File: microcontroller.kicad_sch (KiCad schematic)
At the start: 0 parts

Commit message: top-level structure and ESP32-C6 pin assignments nearly sorted
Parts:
- added BT1: 18650, Battery:BatteryHolder_Keystone_1042_1x18650, symbol Device:Battery_Cell
- added C20: 100n, Capacitor_SMD:C_0603_1608Metric, symbol Device:C
- added J1: Micro_SD_Card 693072010801, Connector_Card:microSD_HC_Molex_47219-2001, symbol Connector:Micro_SD_Card
- added R11, R12: 4K7, Resistor_SMD:R_0603_1608Metric, symbol Device:R
- added R13, R14, R8, R9: 10k, Resistor_SMD:R_0603_1608Metric, symbol Device:R
- added U1: Seeed 113991254, Seeed:XIAO-ESP32-C6-SMD_PTH_DI, symbol OpenPolysom:XIAO-ESP32-C6-SMD
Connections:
- new net 3V3: C20.1, J1.4 (VDD), R11.1, R12.1, R8.1, R9.1, U1.12 (3V3), U1.22 (3V3)
- new net CLK_3: J1.5 (CLK), U1.19 (GPIO4_MTMS)
- new net CS_2: U1.2 (GPIO1_A1_D1)
- new net CS_3: J1.2 (DAT3/CD), U1.3 (GPIO2_A2_D2)
- new net DAT1: J1.8 (DAT1), R9.2
- new net DAT2: J1.1 (DAT2), R8.2
- new net GND: BT1.2 (-), C20.2, J1.6 (VSS), J1.SH (SHIELD), R14.2, U1.13 (GND), U1.18 (GND), U1.24 (GND)
- new net I2S_BCLK: U1.1 (GPIO0_A0_D0)
- new net I2S_DATA: U1.11 (GPIO18_D10_MOSI)
- new net I2S_MCLK: U1.16 (GPIO7_MTDO)
- new net I2S_WS: U1.8 (GPIO17_D7_RX)
- new net MISO_2: U1.10 (GPIO20_D9_MISO)
- new net MISO_3: J1.7 (DAT0), U1.15 (GPIO5_MTDI)
- new net MOSI_2: U1.4 (GPIO21_D3)
- new net MOSI_3: J1.3 (CMD), U1.20 (GPIO6_MTCK)
- new net PERIPH_EN: U1.7 (GPIO16_D6_TX)
- new net SCK_2: U1.9 (GPIO19_D8_SCK)
- new net SCL: R12.2, U1.6 (GPIO23_D5_SCL)
- new net SDA: R11.2, U1.5 (GPIO22_D4_SDA)
- new net VBAT: BT1.1 (+), R13.2, U1.23 (BAT)
- new net VBAT/2: R13.1, R14.1
- new net VBUS: U1.14 (VBUS)
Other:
- company: (none) -> Sunrise designs
- title: (none) -> Open polysomnography board

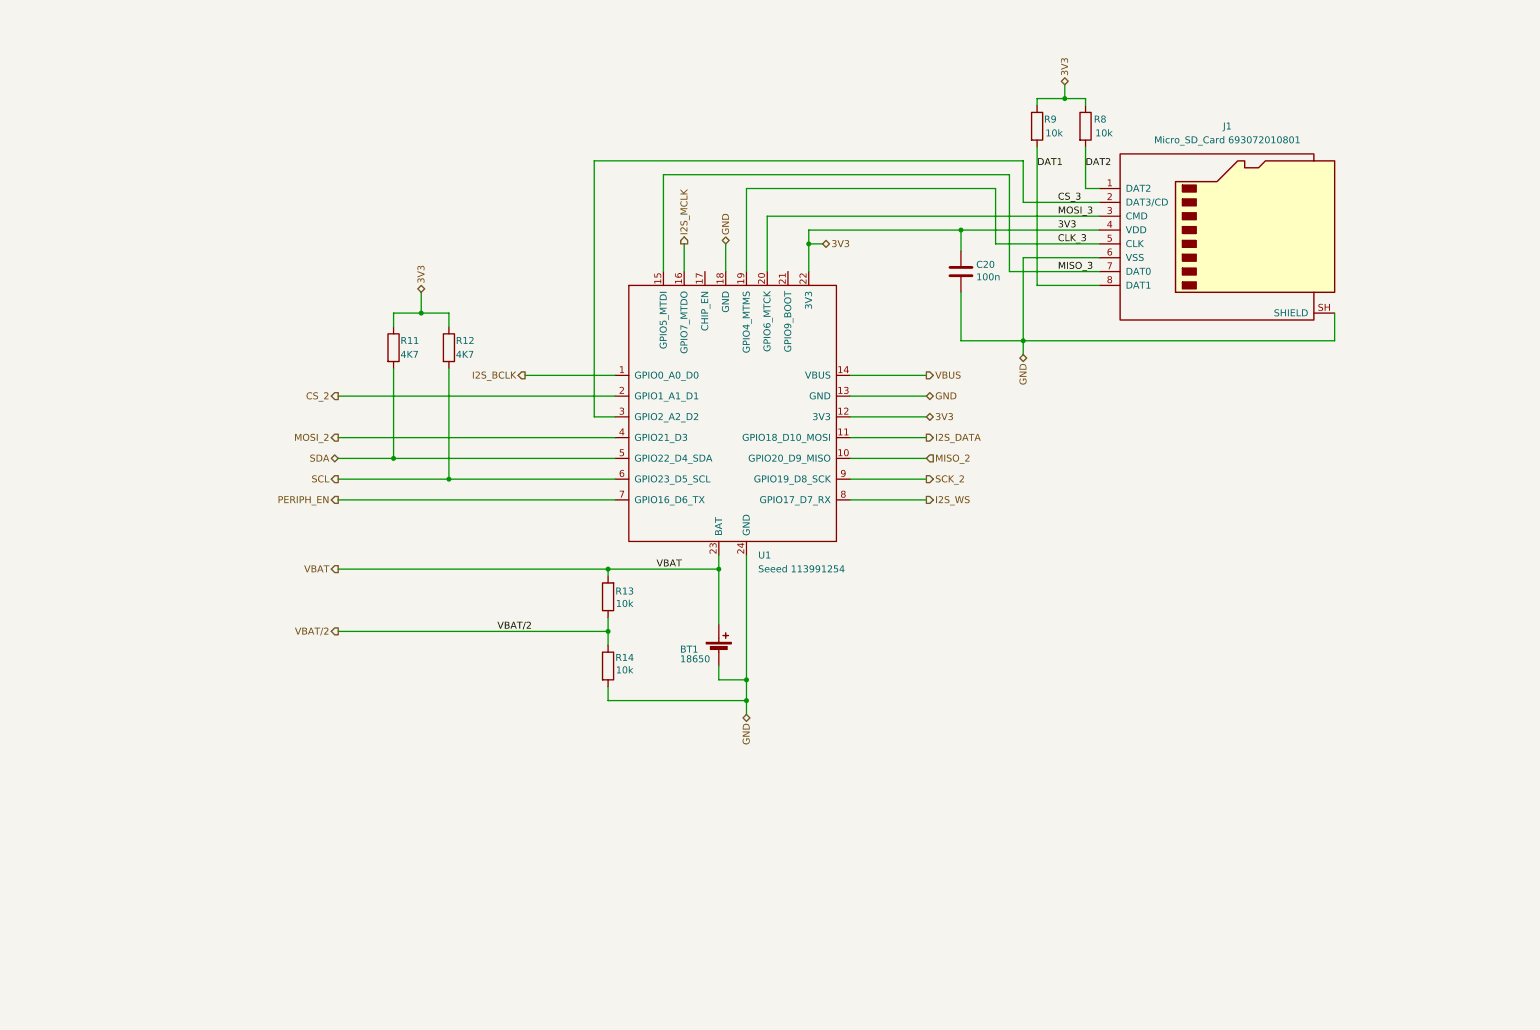
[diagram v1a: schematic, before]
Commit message: text comments sections added
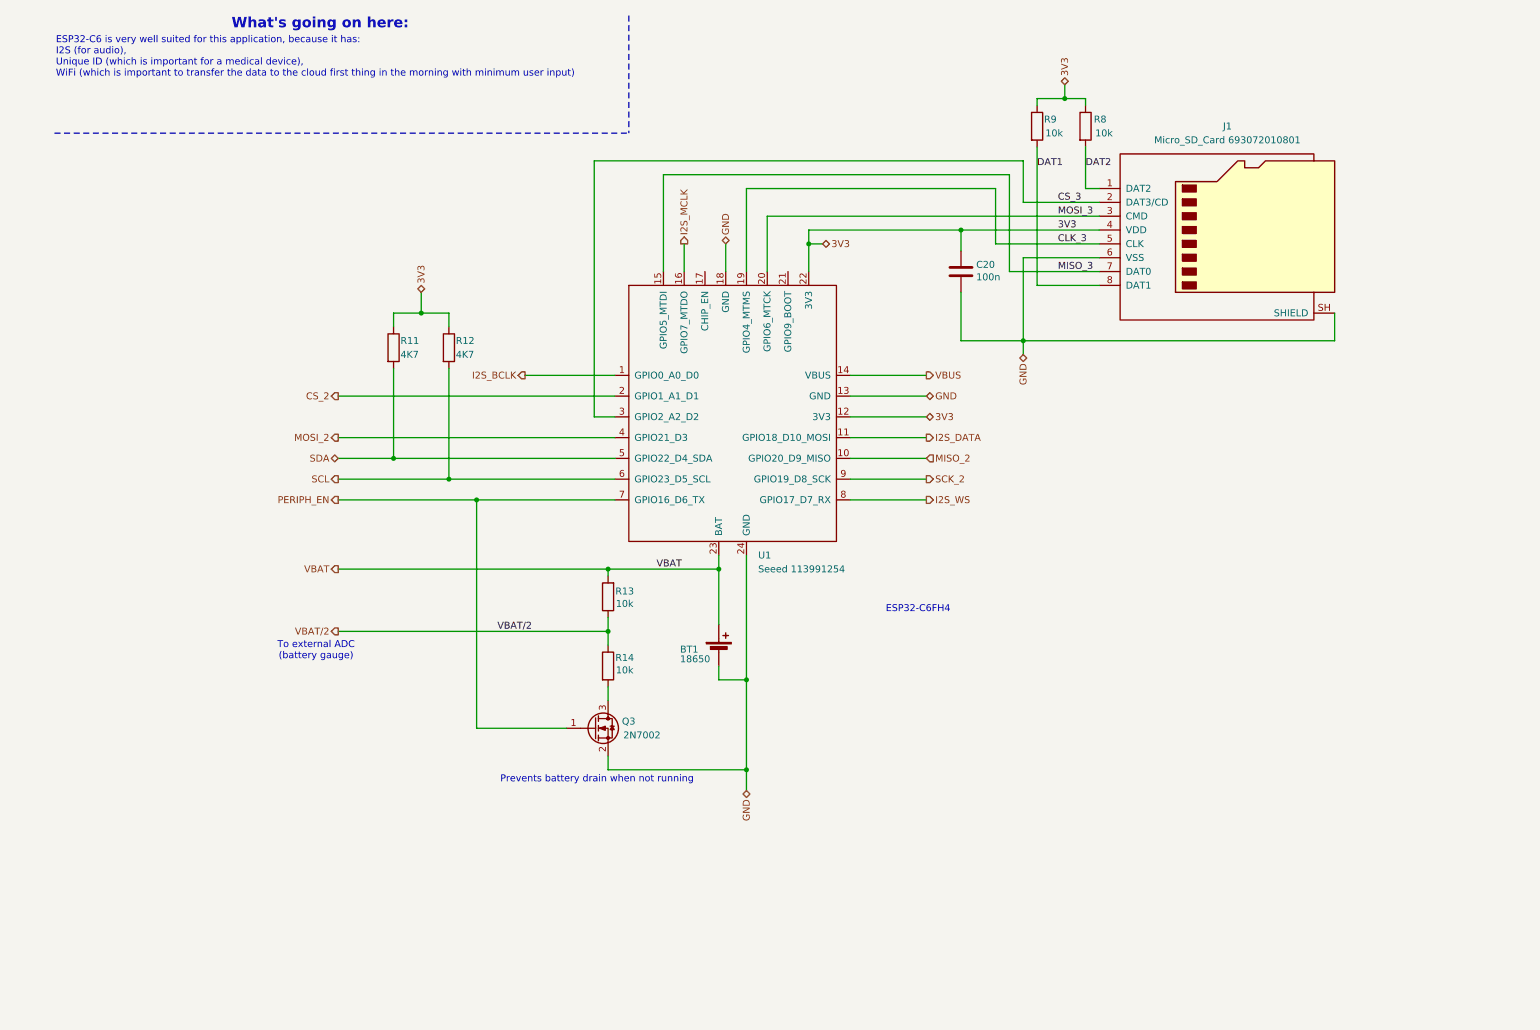
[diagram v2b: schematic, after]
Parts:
- added Q3: 2N7002, Package_TO_SOT_SMD:SOT-23, symbol Transistor_FET:2N7002
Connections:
- net GND: now also Q3.2 (S); no longer R14.2
- net PERIPH_EN: now also Q3.1 (G)
- new net: Q3.3 (D), R14.2
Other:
- note added: "ESP32-C6 is very well suited for this application, because it has: I2S (for audio), Unique ID (which is important for a medical device), WiFi (which is important to transfer the data to the cloud first thing in the morning with minimum user input)"
- note added: "ESP32-C6FH4"
- note added: "Prevents battery drain when not running"
- note added: "To external ADC (battery gauge)"
- note added: "What's going on here:"
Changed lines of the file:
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@@
 		(company "Sunrise designs")
+	)
+	(text "Prevents battery drain when not running\n"
+		(exclude_from_sim no)
+		(at 112.268 152.908 0)
+		(effects
+			(font
+				(size 1.27 1.27)
+			)
+		)
+	)
+	(text "To external ADC\n(battery gauge)"
+		(exclude_from_sim no)
+		(at 60.706 129.286 0)
+		(effects
+			(font
+				(size 1.27 1.27)
+			)
+		)
+	)
+	(text "ESP32-C6FH4"
+		(exclude_from_sim no)
+		(at 171.196 121.666 0)
+		(effects
+			(font
+				(size 1.27 1.27)
+			)
+		)
+	)
+	(text "What's going on here:\n"
+		(exclude_from_sim no)
+		(at 61.468 14.224 0)
+		(effects
+			(font
+				(size 1.905 1.905)
+				(thickness 0.381)
+				(bold yes)
+				(color 132 0 0 1)
+			)
+		)
+	)
+	(text "ESP32-C6 is very well suited for this application, because it has:\nI2S (for audio),\nUnique ID (which is important for a medical device), \nWiFi (which is important to transfer the data to the cloud first thing in the morning with minimum user input)\n"
+		(exclude_from_sim no)
+		(at 12.954 16.51 0)
+		(effects
+			(font
+				(size 1.27 1.27)
+				(color 132 0 0 1)
+			)
+			(justify left top)
+		)
 	)
 	(junction
@@
 	)
 	(junction
-		(at 114.3 125.73)
+		(at 139.7 151.13)
 		(diameter 0)
 		(color 0 0 0 0)
 	)
 	(junction
-		(at 139.7 138.43)
+		(at 114.3 125.73)
 		(diameter 0)
 		(color 0 0 0 0)
@@
 		(color 0 0 0 0)
 	)
+	(junction
+		(at 90.17 101.6)
+		(diameter 0)
+		(color 0 0 0 0)
+	)
+	(wire
+		(pts
+			(xy 114.3 135.89) (xy 114.3 138.43)
+		)
+		(stroke
+			(width 0)
+			(type default)
+		)
+	)
 	(wire
 		(pts
@@
 	(wire
 		(pts
+			(xy 139.7 151.13) (xy 139.7 154.94)
+		)
+		(stroke
+			(width 0)
+			(type default)
+		)
+	)
+	(wire
+		(pts
 			(xy 158.75 101.6) (xy 172.72 101.6)
 		)
@@
 	(wire
 		(pts
+			(xy 114.3 148.59) (xy 114.3 151.13)
+		)
+		(stroke
+			(width 0)
+			(type default)
+		)
+	)
+	(wire
+		(pts
 			(xy 179.07 52.07) (xy 179.07 55.88)
 		)
@@
 	(wire
 		(pts
-			(xy 139.7 134.62) (xy 139.7 138.43)
+			(xy 139.7 134.62) (xy 139.7 151.13)
 		)
 		(stroke
@@
 	(wire
 		(pts
+			(xy 90.17 143.51) (xy 90.17 101.6)
+		)
+		(stroke
+			(width 0)
+			(type default)
+		)
+	)
+	(wire
+		(pts
 			(xy 187.96 41.91) (xy 187.96 59.69)
 		)
@@
 	(wire
 		(pts
+			(xy 90.17 101.6) (xy 115.57 101.6)
+		)
+		(stroke
+			(width 0)
+			(type default)
+		)
+	)
+	(wire
+		(pts
 			(xy 185.42 44.45) (xy 185.42 54.61)
 		)
@@
 	(wire
 		(pts
-			(xy 139.7 138.43) (xy 139.7 140.97)
-		)
-		(stroke
-			(width 0)
-			(type default)
-		)
-	)
-	(wire
-		(pts
 			(xy 190.5 46.99) (xy 204.47 46.99)
 		)
@@
 		)
 	)
+	(polyline
+		(pts
+			(xy 12.7 34.29) (xy 118.11 34.29)
+		)
+		(stroke
+			(width 0)
+			(type dash)
+			(color 132 0 0 1)
+		)
+	)
 	(wire
 		(pts
@@
 		)
 	)
+	(polyline
+		(pts
+			(xy 118.11 12.7) (xy 118.11 34.29)
+		)
+		(stroke
+			(width 0)
+			(type dash)
+			(color 132 0 0 1)
+		)
+	)
 	(wire
 		(pts
@@
 	(wire
 		(pts
-			(xy 114.3 138.43) (xy 139.7 138.43)
+			(xy 114.3 151.13) (xy 139.7 151.13)
 		)
 		(stroke
@@
 	(wire
 		(pts
-			(xy 114.3 135.89) (xy 114.3 138.43)
-		)
-		(stroke
-			(width 0)
-			(type default)
-		)
-	)
-	(wire
-		(pts
 			(xy 179.07 63.5) (xy 179.07 72.39)
 		)
@@
 	(wire
 		(pts
+			(xy 90.17 143.51) (xy 106.68 143.51)
+		)
+		(stroke
+			(width 0)
+			(type default)
+		)
+	)
+	(wire
+		(pts
 			(xy 190.5 72.39) (xy 190.5 74.93)
 		)
@@
 	(wire
 		(pts
-			(xy 64.77 101.6) (xy 115.57 101.6)
+			(xy 64.77 101.6) (xy 90.17 101.6)
 		)
 		(stroke
@@
 	(hierarchical_label "GND"
 		(shape bidirectional)
-		(at 139.7 140.97 270)
+		(at 139.7 154.94 270)
 		(effects
 			(font
@@
 					(unit 1)
 				)
+			)
+		)
+	)
+	(symbol
+		(lib_id "Transistor_FET:2N7002")
+		(at 111.76 143.51 0)
+		(unit 1)
+		(body_style 1)
+		(exclude_from_sim no)
+		(in_bom yes)
+		(on_board yes)
+		(in_pos_files yes)
+		(dnp no)
+		(property "Reference" "Q3"
+			(at 116.84 142.24 0)
+			(show_name no)
+			(do_not_autoplace no)
+			(effects
+				(font
+					(size 1.27 1.27)
+				)
+				(justify left)
+			)
+		)
+		(property "Value" "2N7002"
+			(at 117.094 144.78 0)
+			(show_name no)
+			(do_not_autoplace no)
+			(effects
+				(font
+					(size 1.27 1.27)
+				)
+				(justify left)
+			)
+		)
+		(property "Footprint" "Package_TO_SOT_SMD:SOT-23"
+			(at 116.84 145.415 0)
+			(hide yes)
+			(show_name no)
+			(do_not_autoplace no)
+			(effects
+				(font
+					(size 1.27 1.27)
+					(italic yes)
+				)
+				(justify left)
+			)
+		)
+		(property "Datasheet" "https://www.onsemi.com/pub/Collateral/NDS7002A-D.PDF"
+			(at 116.84 147.32 0)
+			(hide yes)
+			(show_name no)
+			(do_not_autoplace no)
+			(effects
+				(font
+					(size 1.27 1.27)
+				)
+				(justify left)
+			)
+		)
+		(property "Description" "0.115A Id, 60V Vds, N-Channel MOSFET, SOT-23"
+			(at 111.76 143.51 0)
+			(hide yes)
+			(show_name no)
+			(do_not_autoplace no)
+			(effects
+				(font
+					(size 1.27 1.27)
+				)
+			)
+		)
+		(pin "2"
+		)
+		(pin "1"
+		)
+		(pin "3"
+		)
+		(instances
+			(project "Polysom"
+				(path "/1e2e6ca7-e378-49e7-a678-d857aef12e0d/d2ec0716-6a1c-4ede-982f-fa084a578ce0"
+					(reference "Q3")
+					(unit 1)
+				)

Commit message: some work on sch and docs added
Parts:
- removed U1: Seeed 113991254, Seeed:XIAO-ESP32-C6-SMD_PTH_DI, symbol OpenPolysom:XIAO-ESP32-C6-SMD
- added D1, D2: ESD9B5.0ST5G, Diode_SMD:Infineon_SG-WLL-2-3_0.58x0.28_P0.36mm, symbol Diode:ESD9B5.0ST5G
- added D3: SMF5V0A, Diode_SMD:D_SMF, symbol Diode:SMF5V0A
- added J2: USB_C_Receptacle, Connector_USB:USB_C_Receptacle_HRO_TYPE-C-31-M-12, symbol Connector:USB_C_Receptacle
- added R16, R17: 5K1, Resistor_SMD:R_0402_1005Metric, symbol Device:R
- added R18, R19: 0R, Resistor_SMD:R_0402_1005Metric, symbol Device:R
- added R20, R21, R22: 10k, Resistor_SMD:R_0603_1608Metric, symbol Device:R
- added U1: ESP32-C6, Package_DFN_QFN:QFN-40-1EP_5x5mm_P0.4mm_EP3.6x3.6mm, symbol Polysom:ESP32-C6
- added Y1: 32.768kHz, SparkFun-Clock:Crystal_SMD_3.2x1.5mm, symbol SparkFun:Crystal_32.768kHz_3.2x1.5mm
- added Y2: 40MHz, SparkFun-Clock:Crystal_SMD_2.5x2.0mm, symbol SparkFun:Crystal_40MHz_2.5x2.0mm
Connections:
- net MISO_3 is gone; now on net D0: J1.7 (DAT0)
- net 3V3: now also R20.1, R21.1, R22.1
- net GND: now also D1.2 (A2), D2.2 (A2), D3.2 (A2), J2.A1 (GND), J2.A12 (GND), J2.B1 (GND), J2.B12 (GND), J2.SH (SHIELD), R16.1, R17.1, U1.41 (GND)
- net VBUS: now also D3.1 (A1), J2.A4 (VBUS), J2.A9 (VBUS), J2.B4 (VBUS), J2.B9 (VBUS)
- net CLK_3 renamed CLK
- net CS_3 renamed D3
- net D3: now also R20.2
- net DAT1 renamed D0
- net D0: no longer J1.8 (DAT1)
- net DAT2 renamed D2
- net MOSI_3 renamed CMD
- net CMD: now also R21.2
- net PERIPH_EN: no longer names the net of Q3.1 (G)
- net SCL: no longer names the net of R12.2
- net SDA: no longer names the net of R11.2
- net VBAT/2: no longer names the net of R13.1, R14.1
- new net: U1.38 (XTAL_N), Y2.1
- new net: Y2.2, Y2.4
- new net: U1.39 (XTAL_P), Y2.3
- new net: U1.6 (GPIO0/XTAL_32K_P/ADC1_CH0), Y1.1
- new net: U1.7 (GPIO1/XTAL_32K_N/ADC1_CH1), Y1.2
- new net: R18.2, U1.19 (GPIO13/USB_D+)
- new net: J2.B5 (CC2), R17.2
- new net: J2.A5 (CC1), R16.2
- new net: R19.2, U1.18 (GPIO12/USB_D-)
- new net: U1.2 (VDDA3P3), U1.3 (VDDA3P3)
- new net D+: D1.1 (A1), J2.A6 (D+), J2.B6 (D+), R18.1
- new net D-: D2.1 (A1), J2.A7 (D-), J2.B7 (D-), R19.1
- new net D1: J1.8 (DAT1), R22.2
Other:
- note removed: "ESP32-C6FH4"
- moved on the sheet: BT1, C20, J1, Q3, R13, R14, R8, R9
